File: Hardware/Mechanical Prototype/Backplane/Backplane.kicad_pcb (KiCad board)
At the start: 2 copper layers, 240 x 87 mm, 8 parts, among them J201 10018784-10201TLF, J301 10018784-10201TLF, J401 10018784-10201TLF, J501 10018784-10201TLF, J601 10018784-10201TLF, J701 10018784-10201TLF, J801 10018784-10201TLF, J901 10018784-10201TLF

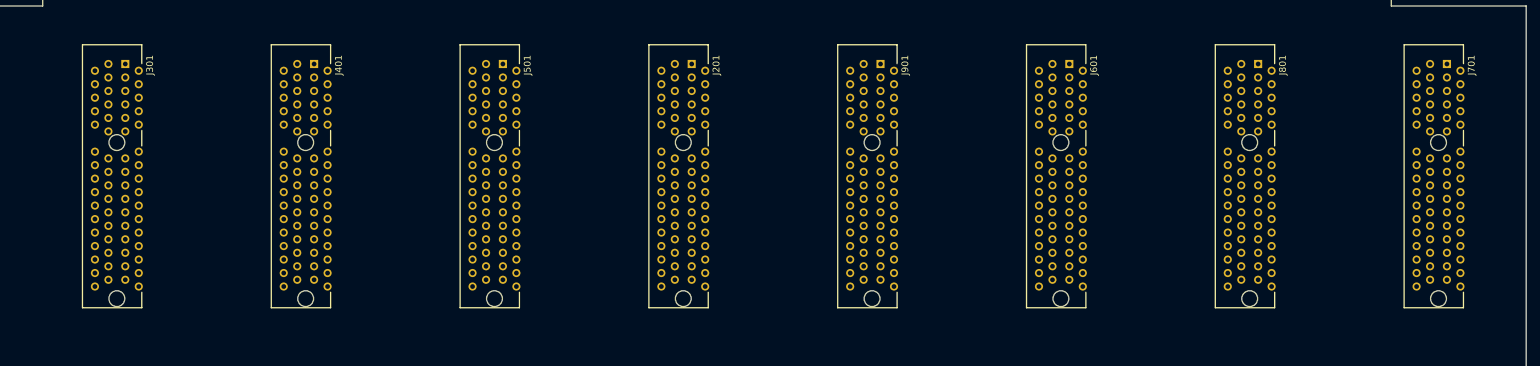
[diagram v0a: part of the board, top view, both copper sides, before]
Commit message: First full draft of mechanical backplane and expansion board design
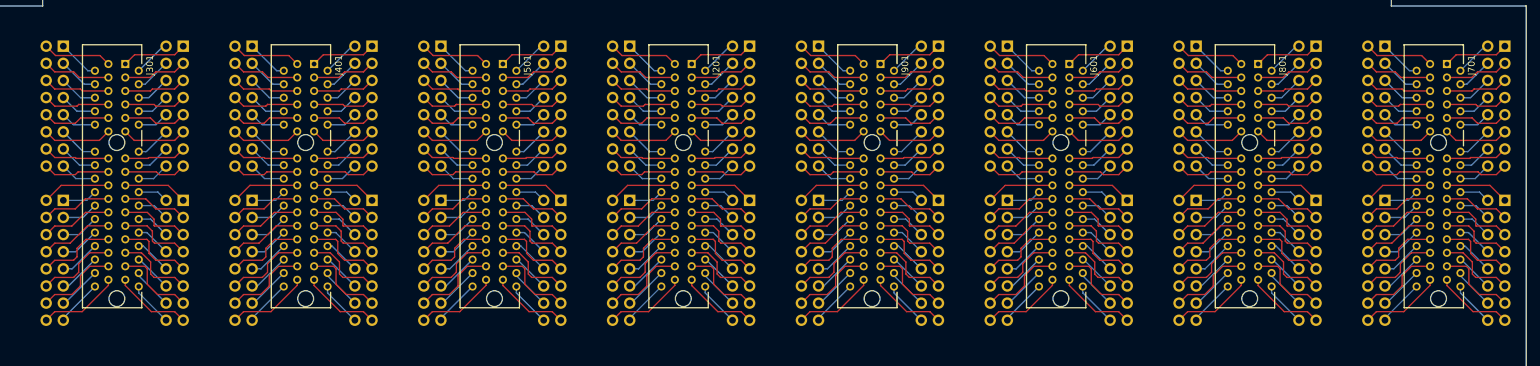
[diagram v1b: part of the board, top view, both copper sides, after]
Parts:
- added J202: Conn_02x08_Odd_Even, Connector_PinHeader_2.54mm:PinHeader_2x08_P2.54mm_Vertical, B.Cu at (155.1, 62.0)
- added J302: Conn_02x08_Odd_Even, Connector_PinHeader_2.54mm:PinHeader_2x08_P2.54mm_Vertical, B.Cu at (71.1, 62.0)
- added J303: Conn_02x08_Odd_Even, Connector_PinHeader_2.54mm:PinHeader_2x08_P2.54mm_Vertical, B.Cu at (155.1, 84.9)
- added J304: Conn_02x08_Odd_Even, Connector_PinHeader_2.54mm:PinHeader_2x08_P2.54mm_Vertical, B.Cu at (71.1, 84.9)
- added J305: Conn_02x08_Odd_Even, Connector_PinHeader_2.54mm:PinHeader_2x08_P2.54mm_Vertical, B.Cu at (99.1, 84.9)
- added J306: Conn_02x08_Odd_Even, Connector_PinHeader_2.54mm:PinHeader_2x08_P2.54mm_Vertical, B.Cu at (127.1, 84.9)
- added J307: Conn_02x08_Odd_Even, Connector_PinHeader_2.54mm:PinHeader_2x08_P2.54mm_Vertical, B.Cu at (211.1, 84.9)
- added J308: Conn_02x08_Odd_Even, Connector_PinHeader_2.54mm:PinHeader_2x08_P2.54mm_Vertical, B.Cu at (267.1, 84.9)
- added J309: Conn_02x08_Odd_Even, Connector_PinHeader_2.54mm:PinHeader_2x08_P2.54mm_Vertical, B.Cu at (239.1, 84.9)
- added J310: Conn_02x08_Odd_Even, Connector_PinHeader_2.54mm:PinHeader_2x08_P2.54mm_Vertical, B.Cu at (183.1, 84.9)
- added J311: Conn_02x08_Odd_Even, Connector_PinHeader_2.54mm:PinHeader_2x08_P2.54mm_Vertical, B.Cu at (137.4, 84.9)
- added J312: Conn_02x08_Odd_Even, Connector_PinHeader_2.54mm:PinHeader_2x08_P2.54mm_Vertical, B.Cu at (53.4, 84.9)
- added J313: Conn_02x08_Odd_Even, Connector_PinHeader_2.54mm:PinHeader_2x08_P2.54mm_Vertical, B.Cu at (81.4, 84.9)
- added J314: Conn_02x08_Odd_Even, Connector_PinHeader_2.54mm:PinHeader_2x08_P2.54mm_Vertical, B.Cu at (109.4, 84.9)
- added J315: Conn_02x08_Odd_Even, Connector_PinHeader_2.54mm:PinHeader_2x08_P2.54mm_Vertical, B.Cu at (193.4, 84.9)
- added J316: Conn_02x08_Odd_Even, Connector_PinHeader_2.54mm:PinHeader_2x08_P2.54mm_Vertical, B.Cu at (249.4, 84.9)
- added J317: Conn_02x08_Odd_Even, Connector_PinHeader_2.54mm:PinHeader_2x08_P2.54mm_Vertical, B.Cu at (221.4, 84.9)
- added J318: Conn_02x08_Odd_Even, Connector_PinHeader_2.54mm:PinHeader_2x08_P2.54mm_Vertical, B.Cu at (165.4, 84.9)
- added J319: Conn_02x08_Odd_Even, Connector_PinHeader_2.54mm:PinHeader_2x08_P2.54mm_Vertical, B.Cu at (137.4, 62.0)
- added J320: Conn_02x08_Odd_Even, Connector_PinHeader_2.54mm:PinHeader_2x08_P2.54mm_Vertical, B.Cu at (53.4, 62.0)
- added J321: Conn_02x08_Odd_Even, Connector_PinHeader_2.54mm:PinHeader_2x08_P2.54mm_Vertical, B.Cu at (81.4, 62.0)
- added J322: Conn_02x08_Odd_Even, Connector_PinHeader_2.54mm:PinHeader_2x08_P2.54mm_Vertical, B.Cu at (109.4, 62.0)
- added J323: Conn_02x08_Odd_Even, Connector_PinHeader_2.54mm:PinHeader_2x08_P2.54mm_Vertical, B.Cu at (193.4, 62.0)
- added J324: Conn_02x08_Odd_Even, Connector_PinHeader_2.54mm:PinHeader_2x08_P2.54mm_Vertical, B.Cu at (249.4, 62.0)
- added J325: Conn_02x08_Odd_Even, Connector_PinHeader_2.54mm:PinHeader_2x08_P2.54mm_Vertical, B.Cu at (221.4, 62.0)
- added J326: Conn_02x08_Odd_Even, Connector_PinHeader_2.54mm:PinHeader_2x08_P2.54mm_Vertical, B.Cu at (165.4, 62.0)
- added J402: Conn_02x08_Odd_Even, Connector_PinHeader_2.54mm:PinHeader_2x08_P2.54mm_Vertical, B.Cu at (99.1, 62.0)
- added J502: Conn_02x08_Odd_Even, Connector_PinHeader_2.54mm:PinHeader_2x08_P2.54mm_Vertical, B.Cu at (127.1, 62.0)
- added J602: Conn_02x08_Odd_Even, Connector_PinHeader_2.54mm:PinHeader_2x08_P2.54mm_Vertical, B.Cu at (211.1, 62.0)
- added J702: Conn_02x08_Odd_Even, Connector_PinHeader_2.54mm:PinHeader_2x08_P2.54mm_Vertical, B.Cu at (267.1, 62.0)
- added J802: Conn_02x08_Odd_Even, Connector_PinHeader_2.54mm:PinHeader_2x08_P2.54mm_Vertical, B.Cu at (239.1, 62.0)
- added J902: Conn_02x08_Odd_Even, Connector_PinHeader_2.54mm:PinHeader_2x08_P2.54mm_Vertical, B.Cu at (183.1, 62.0)
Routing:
- net /Connector 8/B29: track 0.00 -> 12.4 mm
- net /Connector 7/B29: track 0.00 -> 12.4 mm
- net /Connector 6/B29: track 0.00 -> 12.4 mm
- net /Connector 5/B29: track 0.00 -> 12.4 mm
- net /Connector 1/B29: track 0.00 -> 12.4 mm
- net /Connector 4/B29: track 0.00 -> 12.4 mm
- net /Connector 3/B29: track 0.00 -> 12.4 mm
- net /Connector 2/B29: track 0.00 -> 12.4 mm
- net /Connector 6/B31: track 0.00 -> 12.2 mm
- net /Connector 5/B31: track 0.00 -> 12.2 mm
- net /Connector 8/B31: track 0.00 -> 12.2 mm
- net /Connector 7/B31: track 0.00 -> 12.2 mm
- net /Connector 1/B31: track 0.00 -> 12.2 mm
- net /Connector 4/B31: track 0.00 -> 12.2 mm
- net /Connector 3/B31: track 0.00 -> 12.2 mm
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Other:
- board text added: "A1"
- board text added: "A10"
- board text added: "A11"
- board text added: "A12"
- board text added: "A13"
- board text added: "A14"
- board text added: "A15"
- board text added: "A16"
- board text added: "A17"
- board text added: "A18"
- board text added: "A19"
- board text added: "A2"
- board text added: "A20"
- board text added: "A21"
- board text added: "A22"
- board text added: "A23"
- board text added: "A24"
- board text added: "A25"
- board text added: "A26"
- board text added: "A27"
- board text added: "A28"
- board text added: "A29"
- board text added: "A3"
- board text added: "A30"
- board text added: "A31"
- board text added: "A32"
- board text added: "A4"
- board text added: "A5"
- board text added: "A6"
- board text added: "A7"
- board text added: "A8"
- board text added: "A9"
- board text added: "B1"
- board text added: "B10"
- board text added: "B11"
- board text added: "B12"
- board text added: "B13"
- board text added: "B14"
- board text added: "B15"
- board text added: "B16"
- board text added: "B17"
- board text added: "B18"
- board text added: "B19"
- board text added: "B2"
- board text added: "B20"
- board text added: "B21"
- board text added: "B22"
- board text added: "B23"
- board text added: "B24"
- board text added: "B25"
- board text added: "B26"
- board text added: "B27"
- board text added: "B28"
- board text added: "B29"
- board text added: "B3"
- board text added: "B30"
- board text added: "B31"
- board text added: "B32"
- board text added: "B4"
- board text added: "B5"
- board text added: "B6"
- board text added: "B7"
- board text added: "B8"
- board text added: "B9"
